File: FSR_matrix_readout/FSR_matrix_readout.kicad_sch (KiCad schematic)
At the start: 2 parts

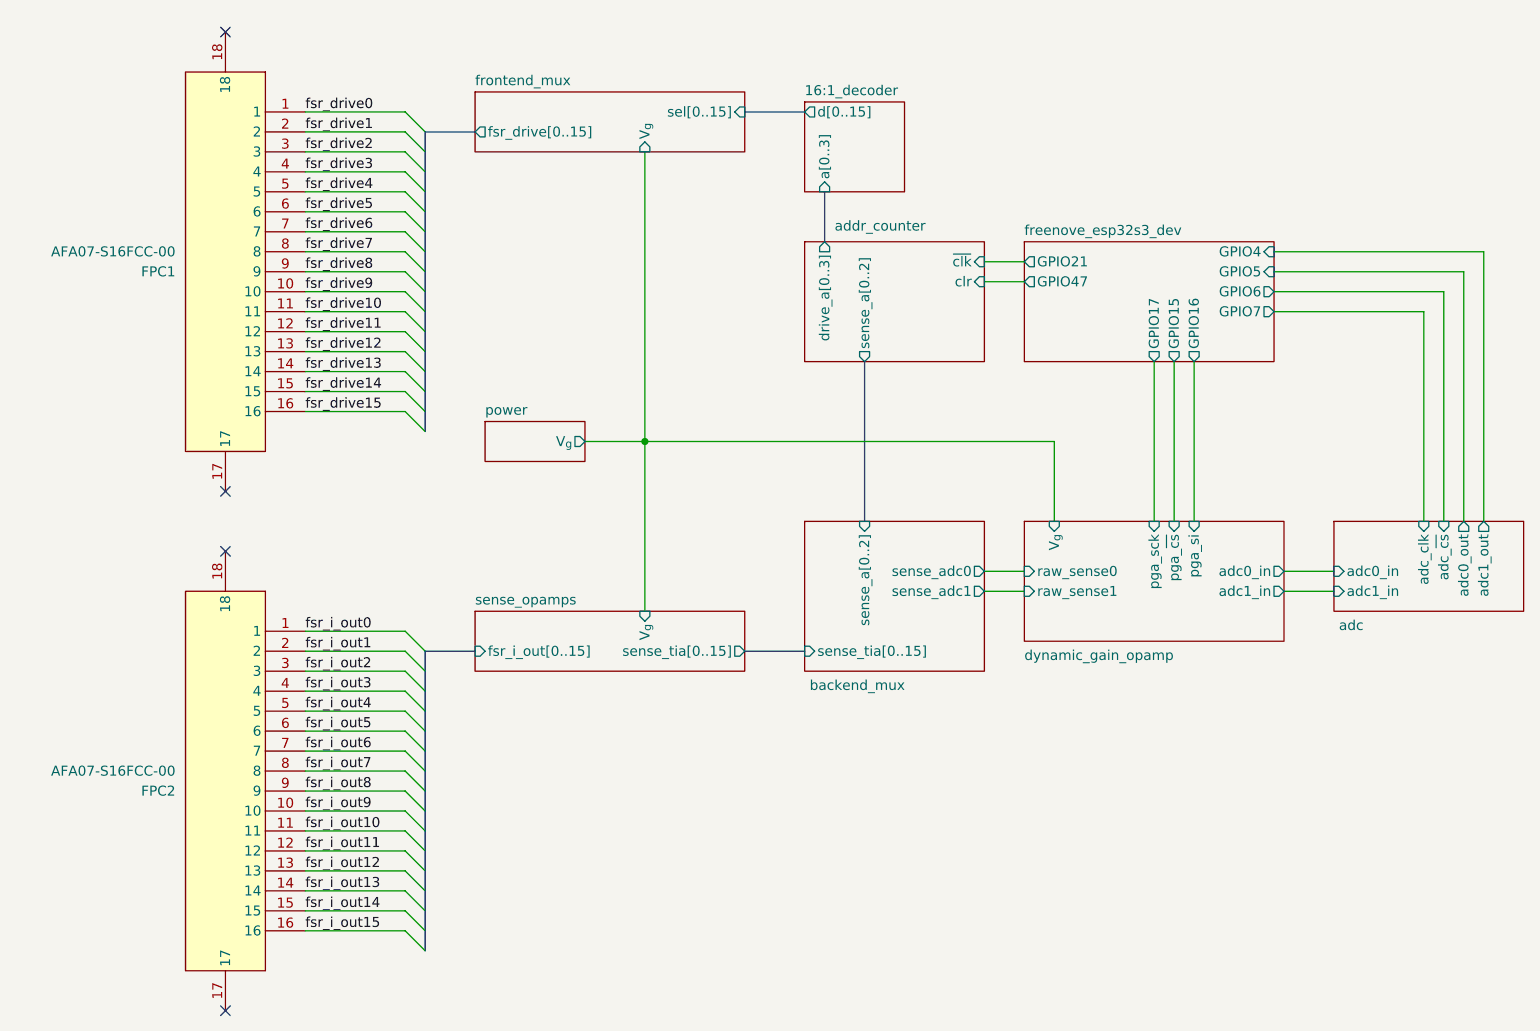
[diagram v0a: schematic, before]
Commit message: added some test points
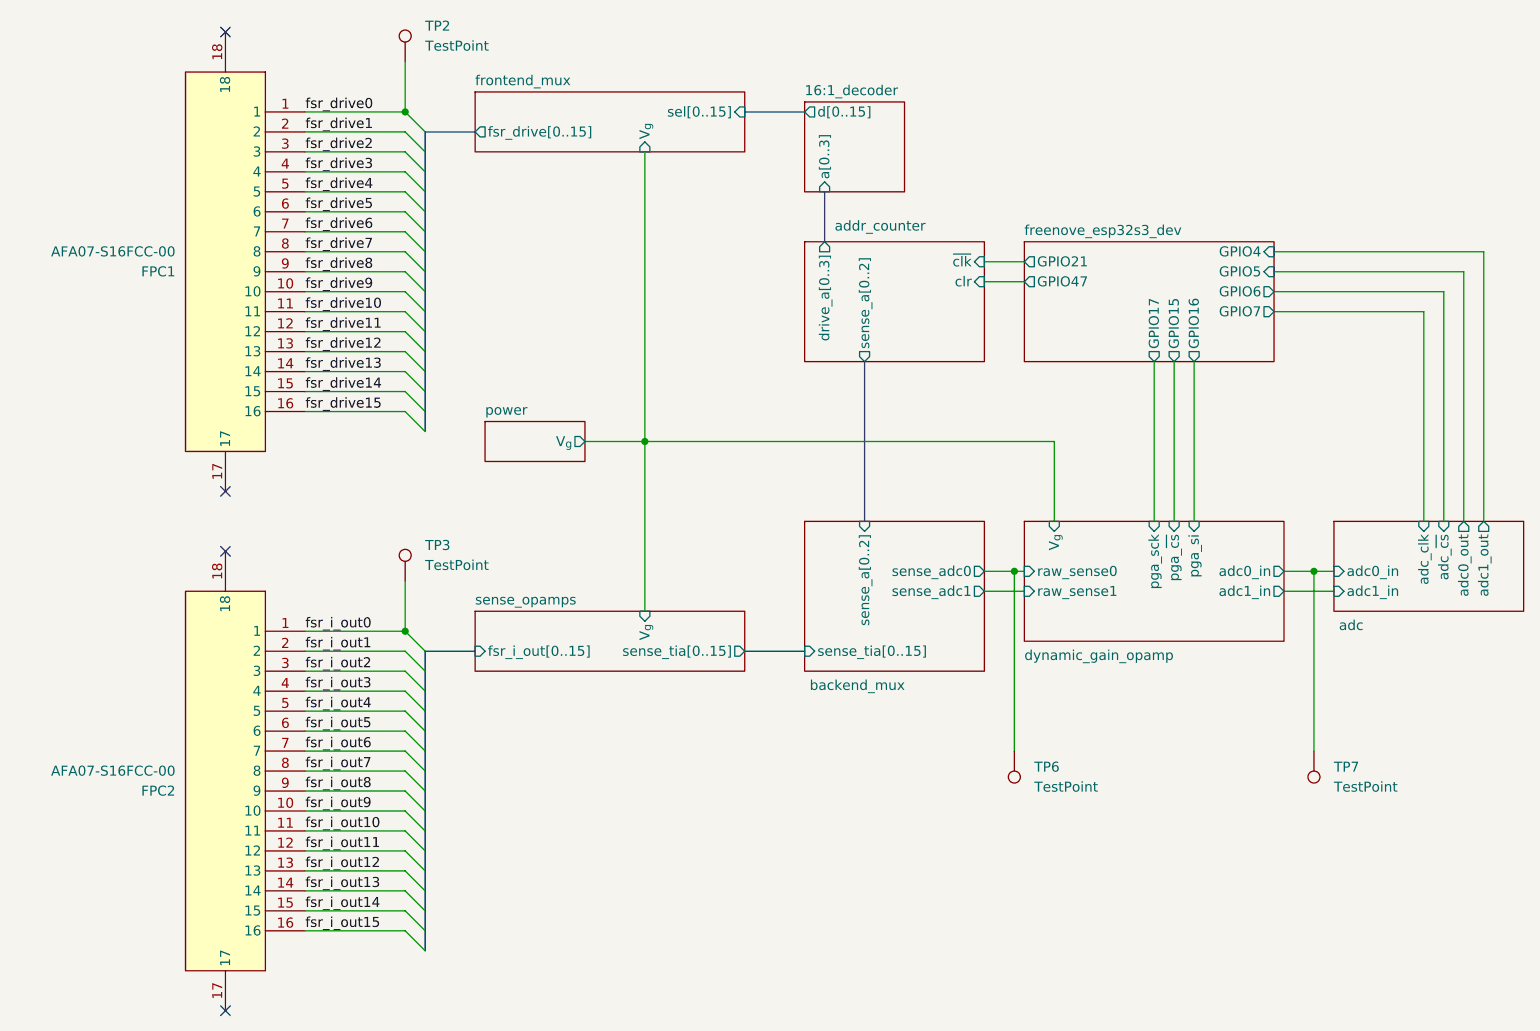
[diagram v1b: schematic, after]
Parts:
- added TP2, TP3, TP6, TP7: TestPoint, symbol Connector:TestPoint
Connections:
- net adc/adc0_in: now also TP7.1
- net backend_mux/sense_adc0: now also TP6.1
- net fsr_drive0: now also TP2.1
- net fsr_i_out0: now also TP3.1
